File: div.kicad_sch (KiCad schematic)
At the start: 6 parts, among them X1 DF40HC_3.0_-100DS-0.4V_58, X2 DF40HC_3.0_-100DS-0.4V_58

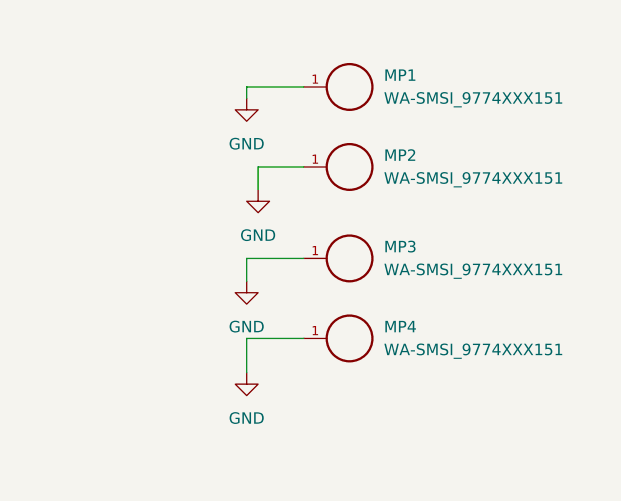
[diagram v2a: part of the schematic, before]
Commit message: Ferdig med modem, + trekke signaler til CM, alt på modem ska vere good nu
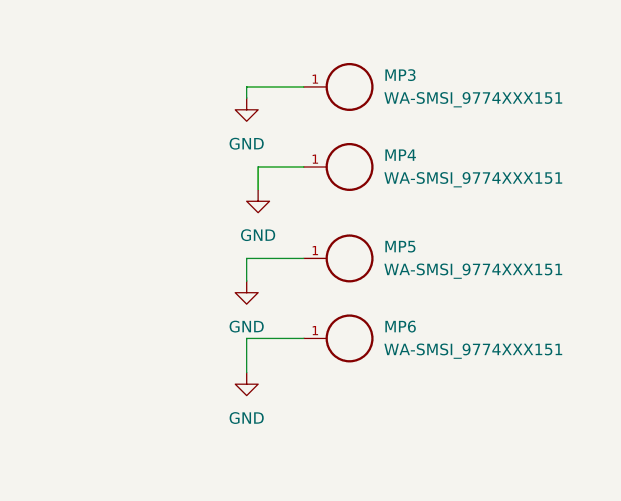
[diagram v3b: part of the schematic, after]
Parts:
- renumbered MP1 to MP3, MP2 to MP4, MP3 to MP5, MP4 to MP6
